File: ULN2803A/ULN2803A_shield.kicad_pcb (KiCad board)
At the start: 2 copper layers, 63.4 x 17.7 mm, 6 parts, among them IC1 ULN2803A, J1 Conn_01x06, J2 Conn_01x06

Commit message: change vreg
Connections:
- net AUX-OUT2 renamed ULN-FAN-OUT
- net AUX-OUT3 renamed ULN-BOOST-OUT
- net AUX-OUT4 renamed ULN-FP-OUT
- net RPM-METER renamed ULN-TACH-OUT

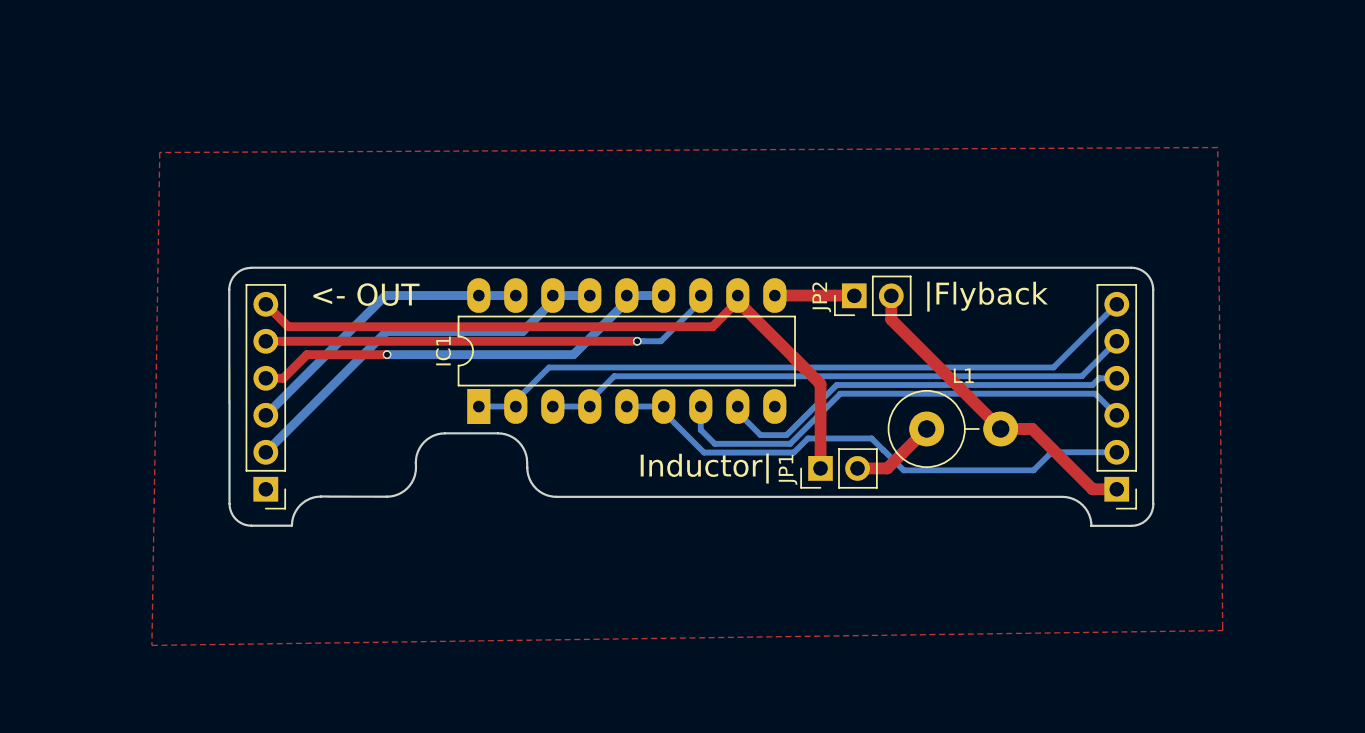
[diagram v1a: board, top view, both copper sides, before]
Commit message: Add mosfet on ULN board
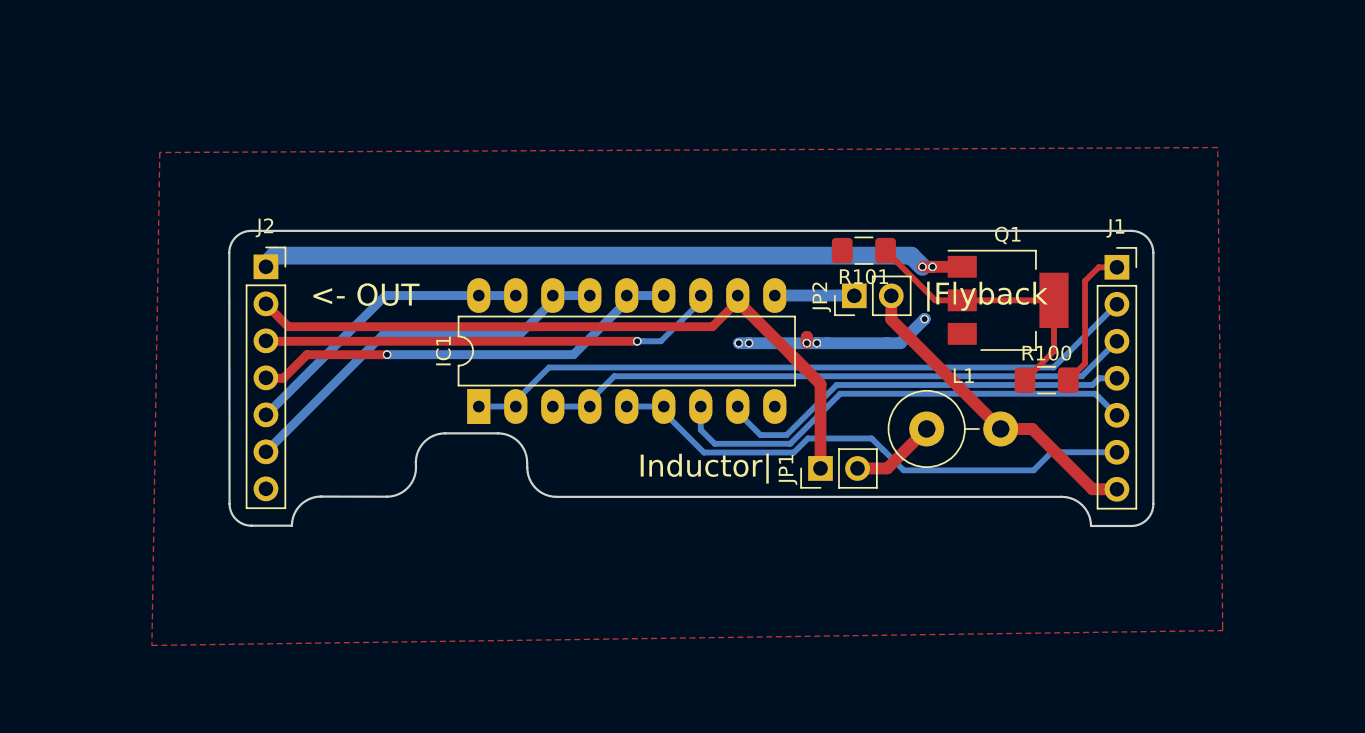
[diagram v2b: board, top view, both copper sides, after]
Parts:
- added Q1: DMN3023L, Package_TO_SOT_SMD:SOT-223-3_TabPin2, F.Cu at (88.8, 97.0)
- added R100: 1k, Resistor_SMD:R_1206_3216Metric_Pad1.42x1.75mm_HandSolder, F.Cu at (91.5, 102.5)
- added R101: 100k, Resistor_SMD:R_1206_3216Metric_Pad1.42x1.75mm_HandSolder, F.Cu at (78.9, 93.6)
- J1, J2: value Conn_01x06 -> Conn_01x07_Male; footprint Pin_Headers:Pin_Header_Straight_1x06_Pitch2.54mm -> Connector_PinSocket_2.54mm:PinSocket_1x07_P2.54mm_Vertical
- moved J2 15.3 mm to (37.9, 94.7), turned to 0 degrees
- moved J1 15.2 mm to (96.3, 94.8), turned to 0 degrees
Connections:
- IC1 pad 13: ULN-BOOST-OUT -> ULN-FAN2-OUT
- IC1 pad 14: ULN-BOOST-OUT -> ULN-FAN2-OUT
- IC1 pad 15: AUX-OUT1 -> ULN-AUX1-OUT
- IC1 pad 16: AUX-OUT1 -> ULN-AUX1-OUT
- J1 pad 1: 12V -> Net-(J1-Pad1)
- J1 pad 2: Net-(IC1-Pad5) -> Net-(IC1-Pad1)
- J1 pad 3: Net-(IC1-Pad7) -> Net-(IC1-Pad3)
- J1 pad 5: Net-(IC1-Pad3) -> Net-(IC1-Pad7)
- J1 pad 6: Net-(IC1-Pad1) -> Net-(IC1-Pad5)
- J2 pad 1: GND -> ULN-BOOST-OUT
- J2 pad 2: AUX-OUT1 -> ULN-TACH-OUT
- J2 pad 3: ULN-FAN-OUT -> ULN-FP-OUT
- J2 pad 4: ULN-BOOST-OUT -> ULN-FAN2-OUT
- J2 pad 5: ULN-FP-OUT -> ULN-FAN-OUT
- J2 pad 6: ULN-TACH-OUT -> ULN-AUX1-OUT
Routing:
- net ULN-FAN2-OUT: track 0.00 -> 29.9 mm, vias 0 -> 1
- net AUX-OUT1: track 26.9 -> 0.00 mm
- net ULN-AUX1-OUT: track 0.00 -> 26.9 mm
- net Net-(Q1-Pad2): track 0.00 -> 19.4 mm
- net ULN-BOOST-OUT: track 29.9 -> 49.2 mm, vias 1 -> 2
- net GND: track 0.00 -> 13.9 mm, vias 0 -> 5
- net Net-(J1-Pad1): track 0.00 -> 9.87 mm
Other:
- board size 63.4 x 17.7 mm -> 63.4 x 20.3 mm

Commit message: Updated bom and footprint in ULN
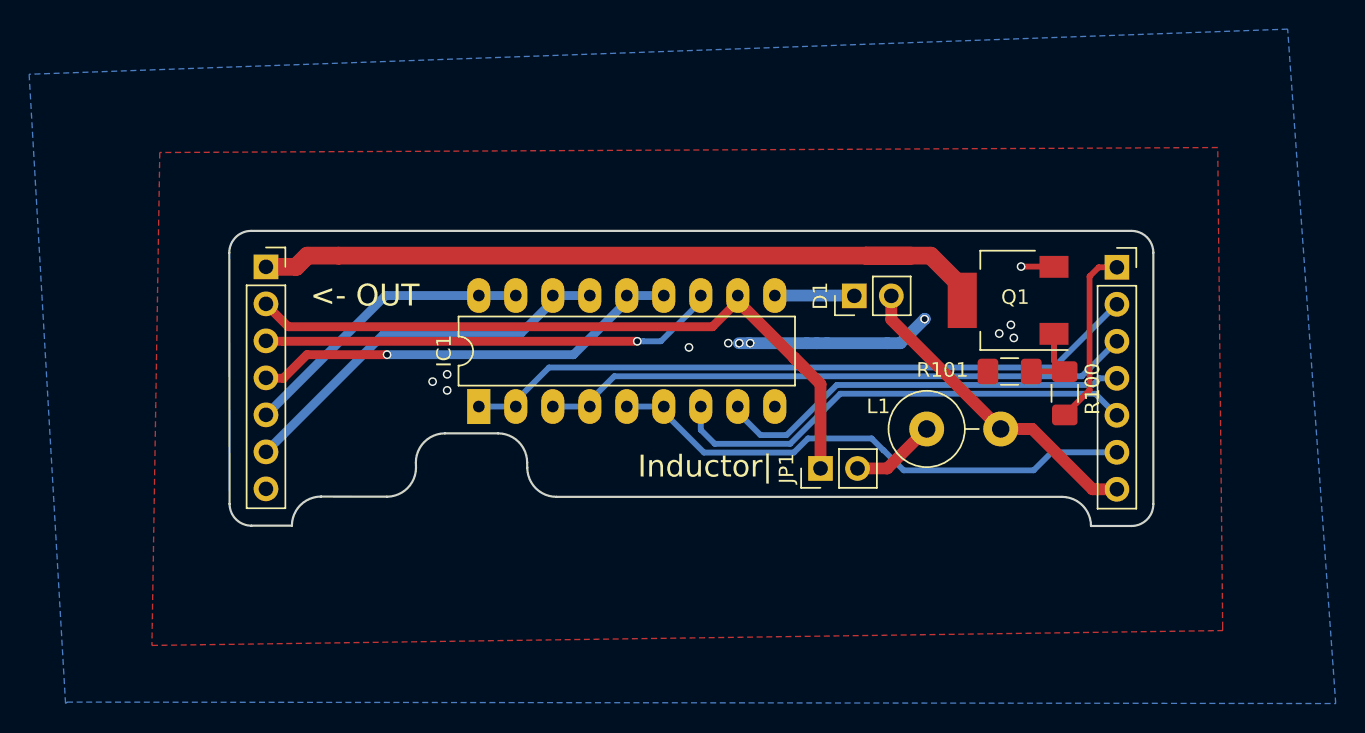
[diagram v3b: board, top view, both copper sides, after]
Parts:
- moved R101 13.0 mm to (88.9, 101.9)
- moved R100 1.54 mm to (92.7, 103.4), turned to 270 degrees
- turned Q1 to 180 degrees
- renumbered JP2 to D1
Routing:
- net Net-(Q1-Pad2): track 19.4 -> 5.20 mm
- net ULN-BOOST-OUT: track 49.2 -> 53.2 mm, vias 2 -> 0
- net Net-(J1-Pad1): track 9.87 -> 12.4 mm
- net GND: track 13.9 -> 15.7 mm, vias 5 -> 12
- added copper zone on B.Cu, net GND
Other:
- board text removed: "|Flyback"
